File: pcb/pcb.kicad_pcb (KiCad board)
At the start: 2 copper layers, 110 x 124 mm, 64 parts, among them J1 AMT0440007DB0000G, J10 Conn_02x10_Odd_Even, J11 Conn_01x03, J12 Conn_01x02, J14 Conn_01x04, J15 Conn_01x10, J16 Conn_01x10, J2 AMT0440007DB0000G, J3 AMT0440007DB0000G, J4 AMT0440007DB0000G, J5 Conn_01x03, J6 Conn_01x03, J7 Conn_01x03, J8 Conn_01x03, J9 Conn_01x03, Q1 IRF9Z34NPBF, Q2 IRF9Z34NPBF, Q3 IRF9Z34NPBF, Q4 IRF9Z34NPBF, Q5 IRF9Z34NPBF, U1 ACS711ELCTR-12AB-T, U2 ACS711ELCTR-12AB-T, U3 ACS711ELCTR-12AB-T, U4 ACS711ELCTR-12AB-T, U5 ACS711ELCTR-12AB-T, U6 TXS0102DCUR, U7 TXS0102DCUR, U8 TXS0102DCUR, U9 NCP718BSNADJT1G

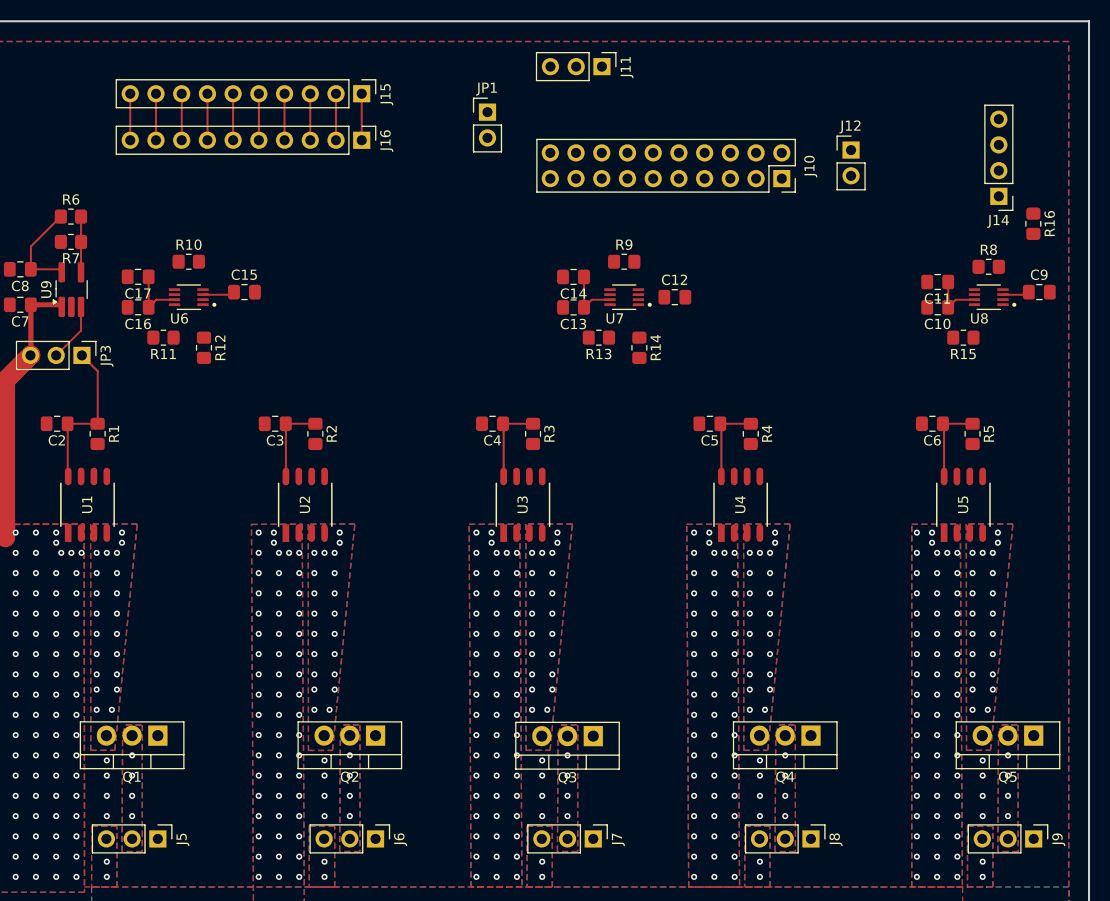
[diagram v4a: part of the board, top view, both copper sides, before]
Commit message: Add traces for PMOSFET shutdown and ctrl signals
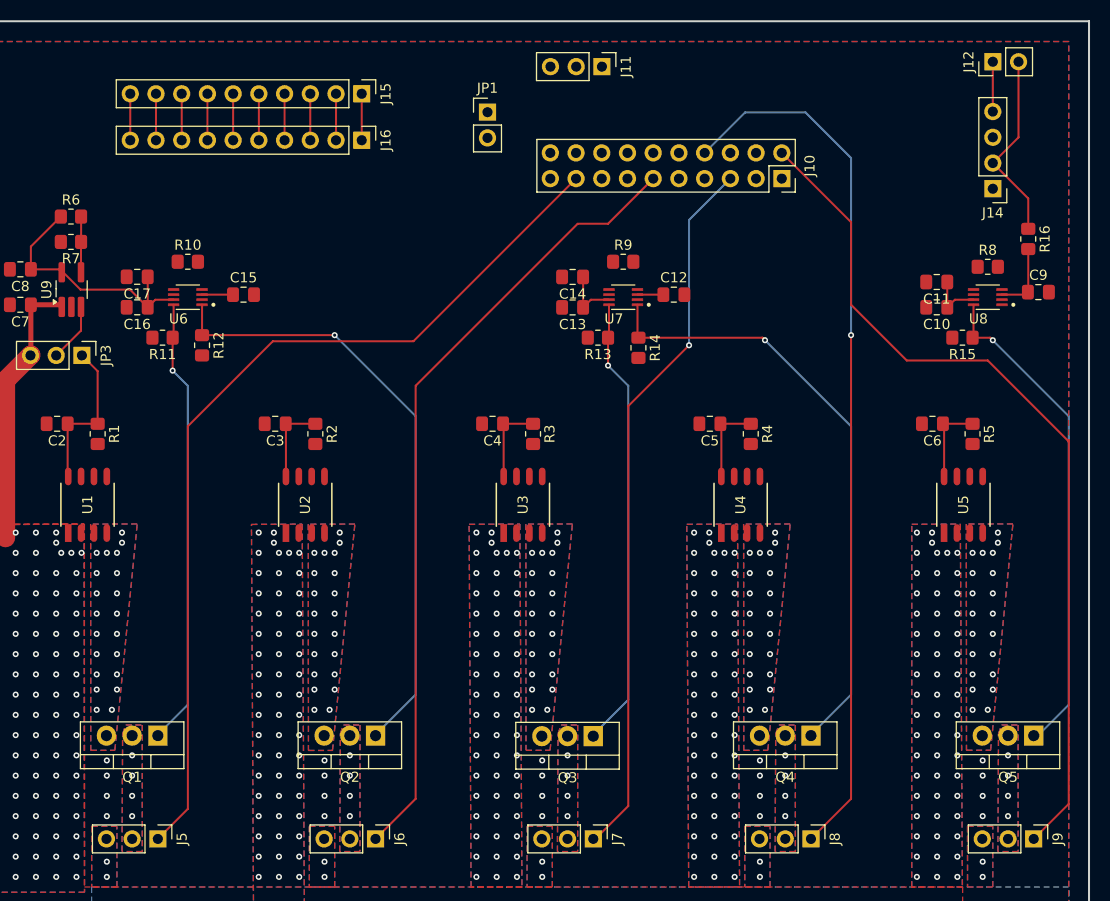
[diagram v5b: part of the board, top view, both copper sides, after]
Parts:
- moved J12 16.5 mm to (192.5, 29.5), turned to 90 degrees
- moved R16 1.58 mm to (196.0, 47.0)
- moved J14 0.96 mm to (192.5, 42.0)
- moved R12 0.31 mm to (114.4, 57.5)
- moved C12 0.27 mm to (161.0, 52.5)
- moved C15 0.27 mm to (118.5, 52.5)
- moved C10 0.09 mm to (187.0, 53.8)
- moved C11 0.09 mm to (187.0, 51.2)
- moved C13 0.09 mm to (151.0, 53.8)
- moved C14 0.09 mm to (151.0, 50.8)
- moved C16 0.09 mm to (108.0, 53.8)
- moved C17 0.09 mm to (108.0, 50.7)
- moved C9 0.09 mm to (197.0, 52.2)
- moved R10 0.09 mm to (113.0, 49.2)
- moved R11 0.09 mm to (110.5, 56.8)
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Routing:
- net CTRL_HIP: track 0.00 -> 90.4 mm
- net CTRL_WRIST: track 0.00 -> 86.9 mm, vias 0 -> 1
- net CTRL_SHOULDER: track 0.00 -> 85.8 mm
- net CTRL_HAND: track 0.00 -> 78.3 mm
- net CTRL_ELBOW: track 0.00 -> 70.9 mm, vias 0 -> 1
- net SHUTOFF_HAND_H: track 0.00 -> 60.6 mm, vias 0 -> 1
- net SHUTOFF_WRIST_H: track 0.00 -> 60.1 mm, vias 0 -> 1
- net SHUTOFF_SHOULDER_H: track 0.00 -> 49.3 mm, vias 0 -> 1
- net SHUTOFF_ELBOW_H: track 0.00 -> 44.8 mm, vias 0 -> 1
- net SHUTOFF_HIP_H: track 0.00 -> 44.4 mm, vias 0 -> 1
- net +DC_OK: track 0.00 -> 19.0 mm
- net +5V: track 26.8 -> 36.7 mm
- net +3V3: track 54.2 -> 60.9 mm
- net +PWR_CTRL: track 0.00 -> 4.92 mm

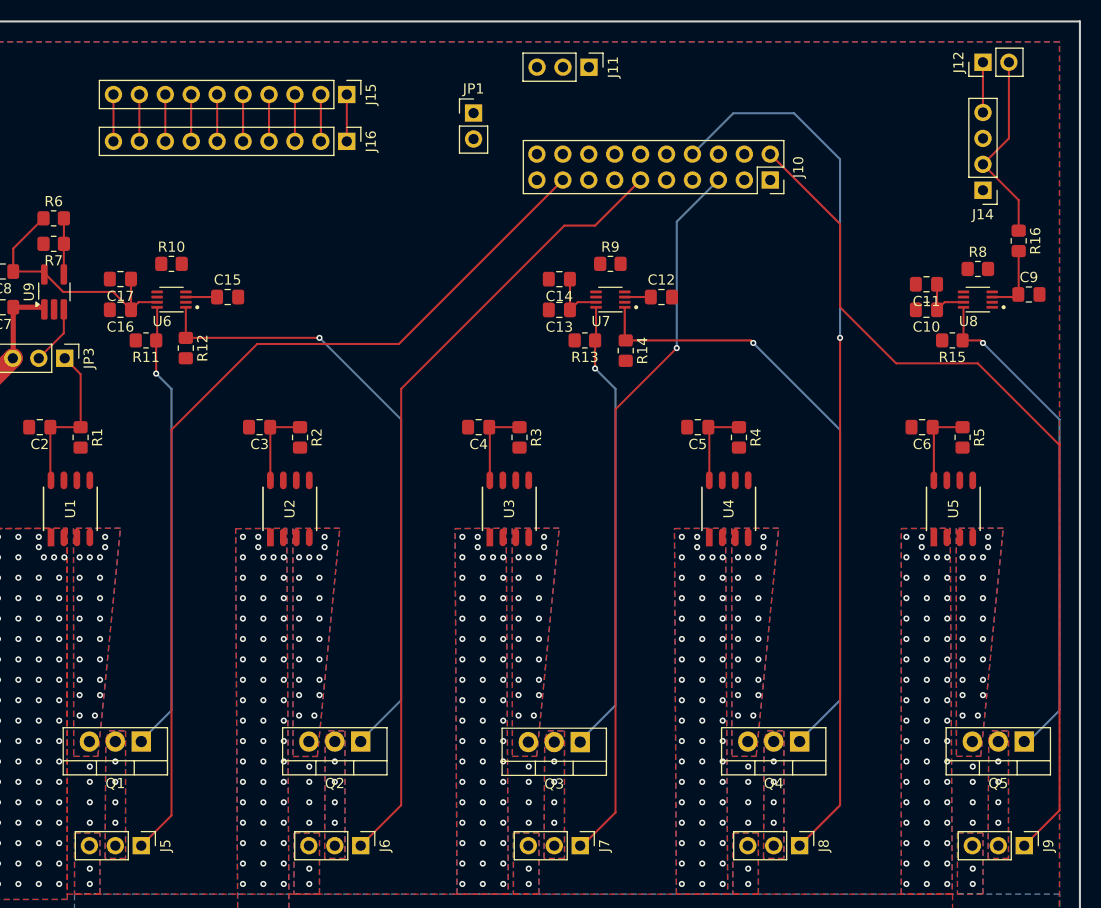
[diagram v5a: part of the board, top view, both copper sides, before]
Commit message: Add traces for Hall effect ICs and +3.3V supply
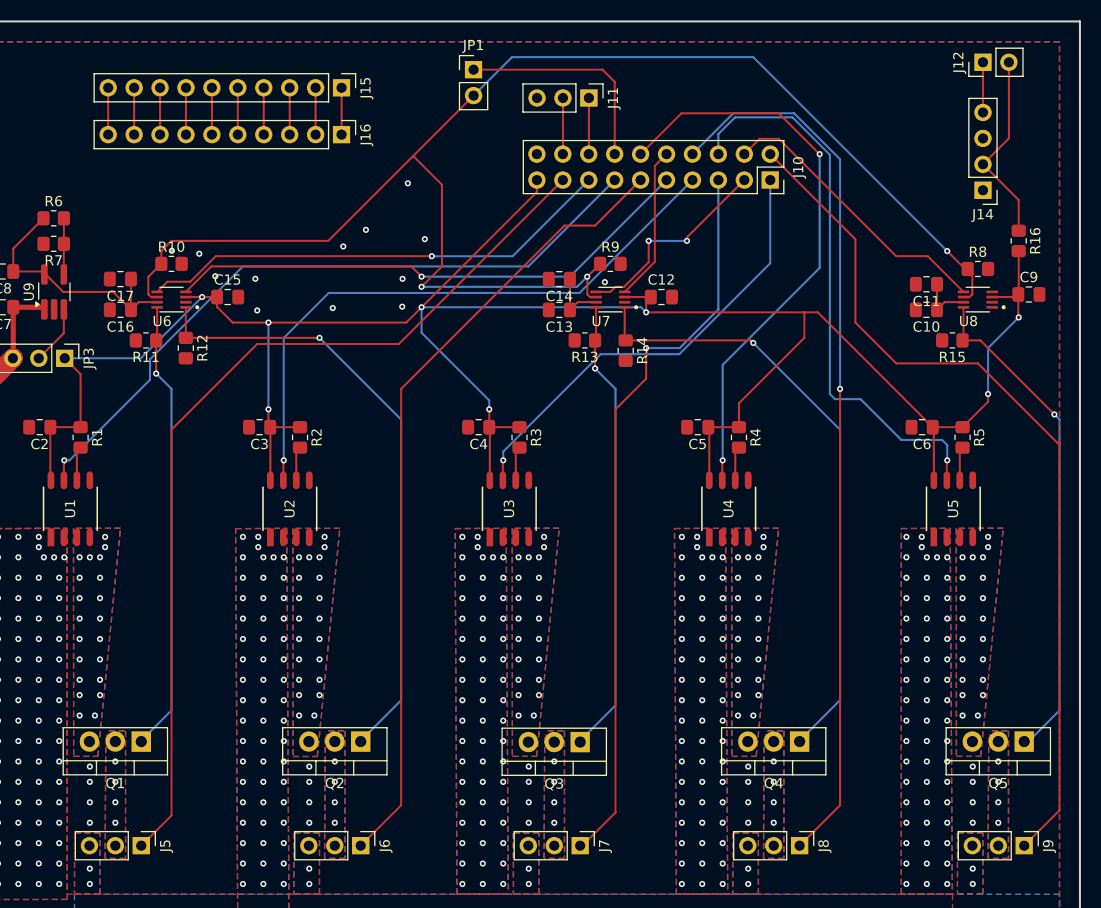
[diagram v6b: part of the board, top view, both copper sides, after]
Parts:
- moved JP1 4.25 mm to (142.6, 30.2)
- moved J11 3.02 mm to (153.9, 33.0)
- moved J15 0.84 mm to (129.7, 32.0)
- moved J16 0.84 mm to (129.7, 36.6)
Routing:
- net +3V3: track 60.9 -> 226.9 mm, vias 0 -> 8
- net LVL_SHIFTER_EN: track 0.00 -> 140.8 mm, vias 0 -> 3
- net I_SENSE_HIP: track 0.00 -> 68.4 mm, vias 0 -> 1
- net I_SENSE_HAND: track 0.00 -> 60.4 mm, vias 0 -> 1
- net I_SENSE_WRIST: track 0.00 -> 56.8 mm, vias 0 -> 2
- net I_SENSE_SHOULDER: track 0.00 -> 55.6 mm, vias 0 -> 1
- net SHUTOFF_HAND_L: track 0.00 -> 52.5 mm, vias 0 -> 1
- net SHUTOFF_HIP_L: track 0.00 -> 46.8 mm, vias 0 -> 1
- net I_SENSE_ELBOW: track 0.00 -> 44.8 mm, vias 0 -> 1
- net SHUTOFF_SHOULDER_L: track 0.00 -> 28.3 mm
- net Net-(J10-Pin_14): track 0.00 -> 21.4 mm
- net SHUTOFF_ELBOW_L: track 0.00 -> 20.5 mm, vias 0 -> 2
- net SHUTOFF_WRIST_L: track 0.00 -> 15.2 mm
- net UART_STM_RX: track 0.00 -> 5.51 mm
- net UART_STM_TX: track 0.00 -> 5.51 mm
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
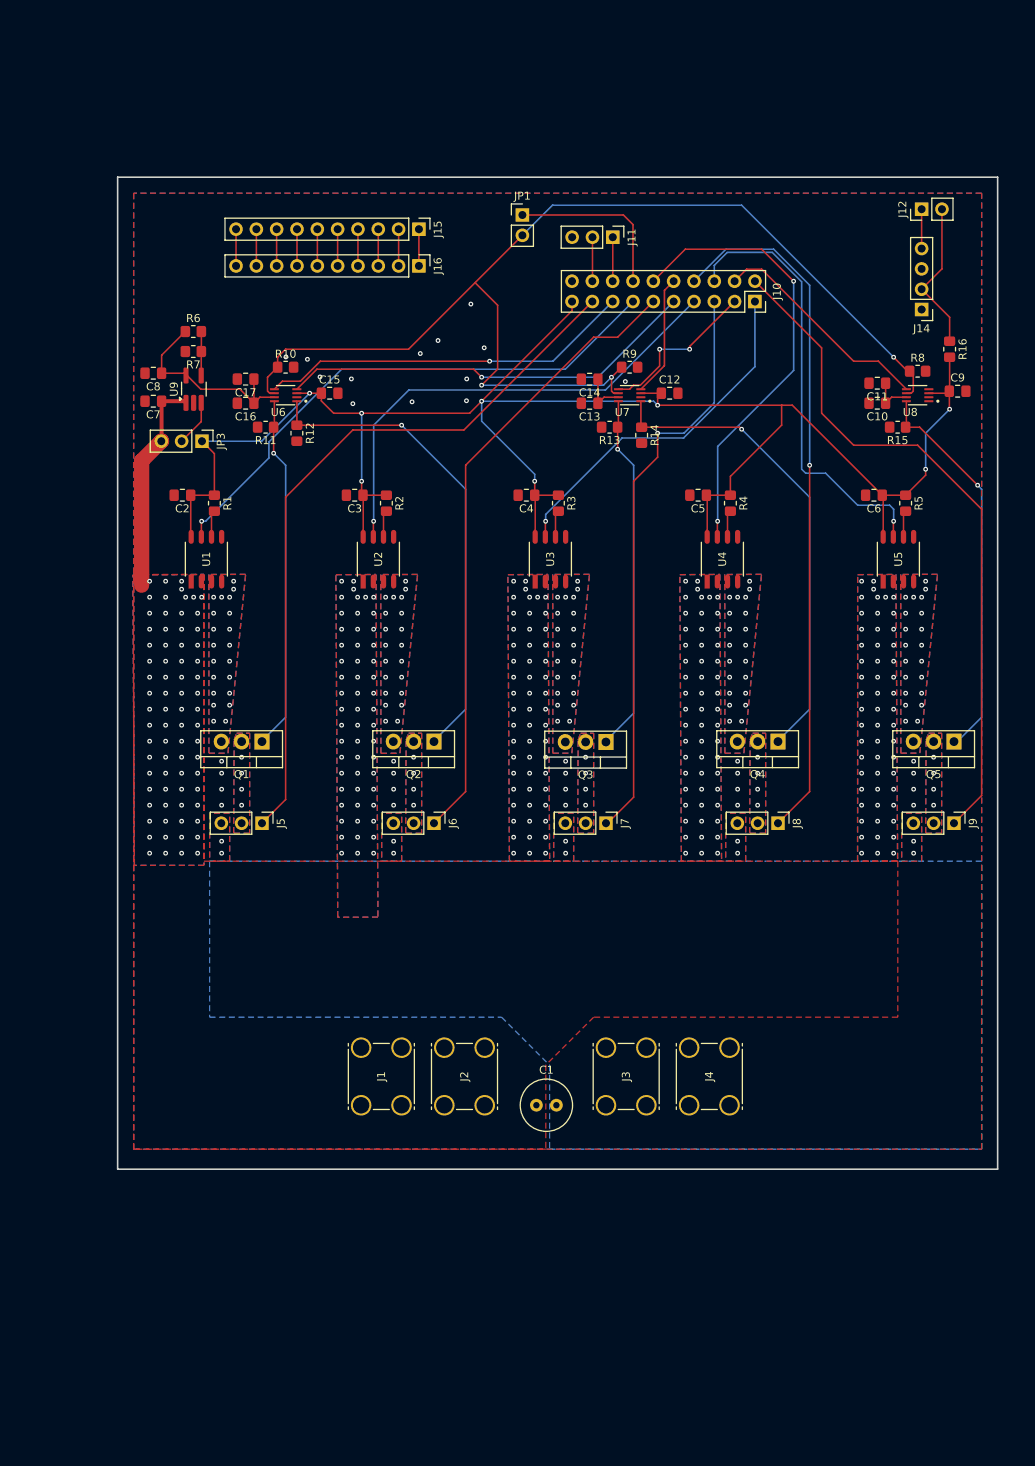
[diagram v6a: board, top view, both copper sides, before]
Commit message: Add +5V supply traces and stitching vias
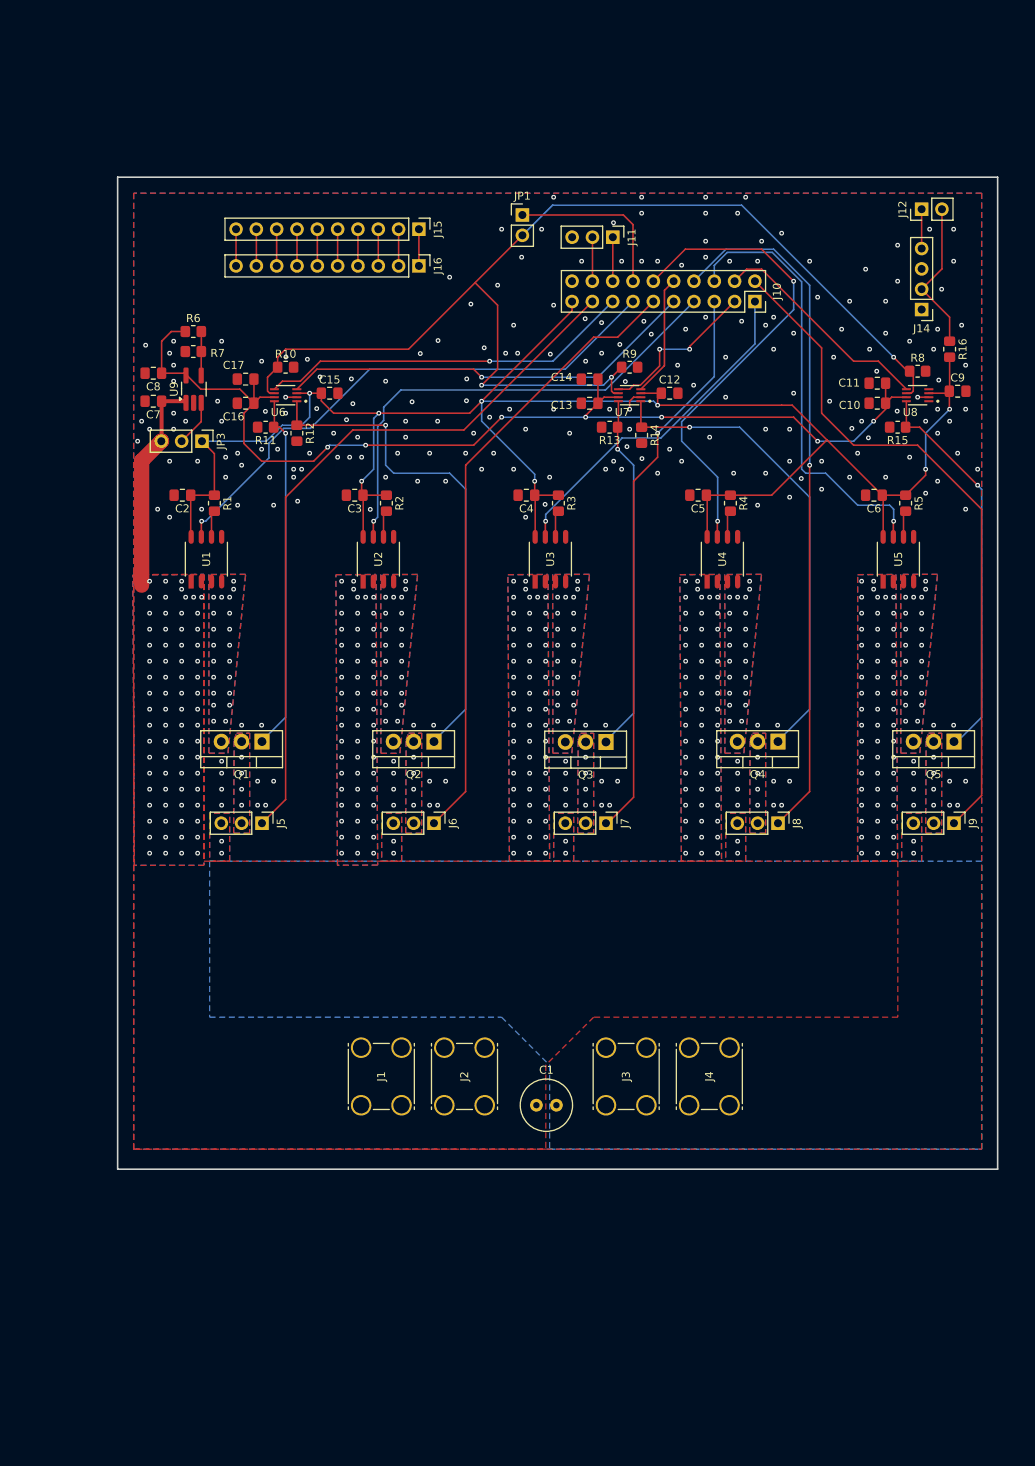
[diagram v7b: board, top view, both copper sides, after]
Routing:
- net +5V: track 36.7 -> 132.7 mm, vias 0 -> 7
- net GNDREF: track 0.00 -> 5.42 mm, vias 43 -> 252
- net I_SENSE_WRIST: track 56.8 -> 60.5 mm
- net +3V3: track 226.9 -> 230.6 mm
- net SHUTOFF_HAND_H: track 60.6 -> 63.5 mm
- net CTRL_ELBOW: track 72.9 -> 70.9 mm
- net I_SENSE_ELBOW: track 44.8 -> 43.1 mm
- net I_SENSE_HAND: track 60.4 -> 61.0 mm
